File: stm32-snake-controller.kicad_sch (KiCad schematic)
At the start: 46 parts, among them J101 Tag Connector, J102 USB_B_Micro, J103 JST 2.54 Header, J107 Conn_01x02, Q101 AO3501A, SW106 SW_Push, U101 STM32F401RCTx, U102 USBLC6-2SC6, U104 M24C64-RMN, Y101 16MHz, Y103 32.768kHz

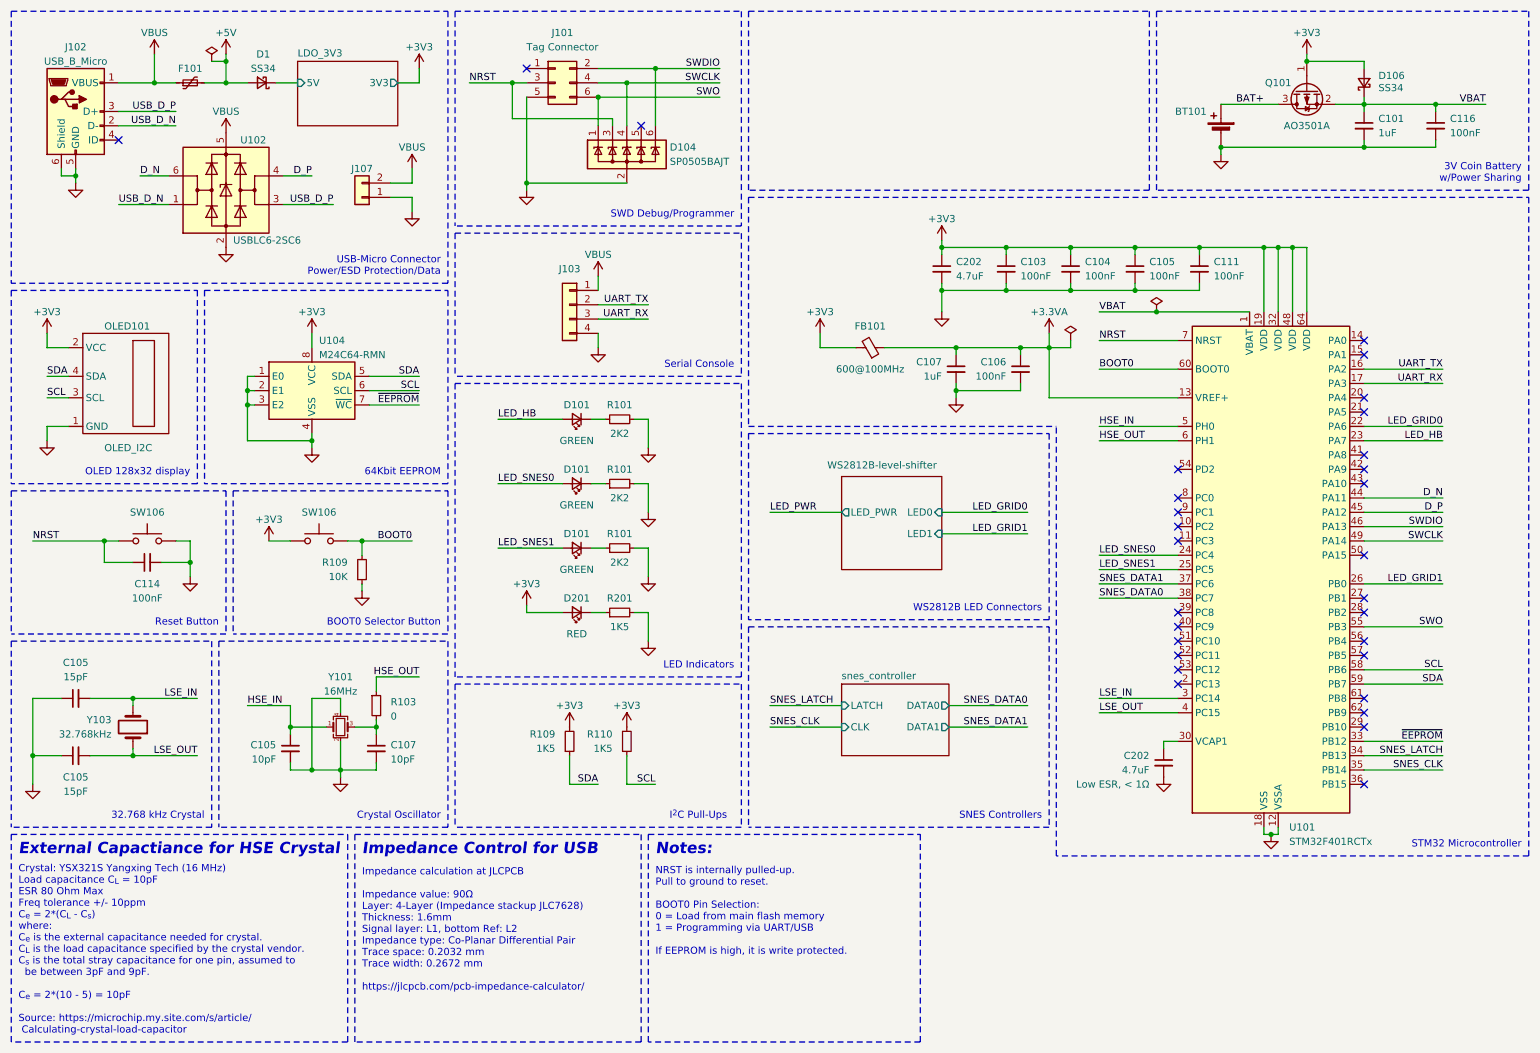
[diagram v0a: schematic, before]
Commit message: update schematic
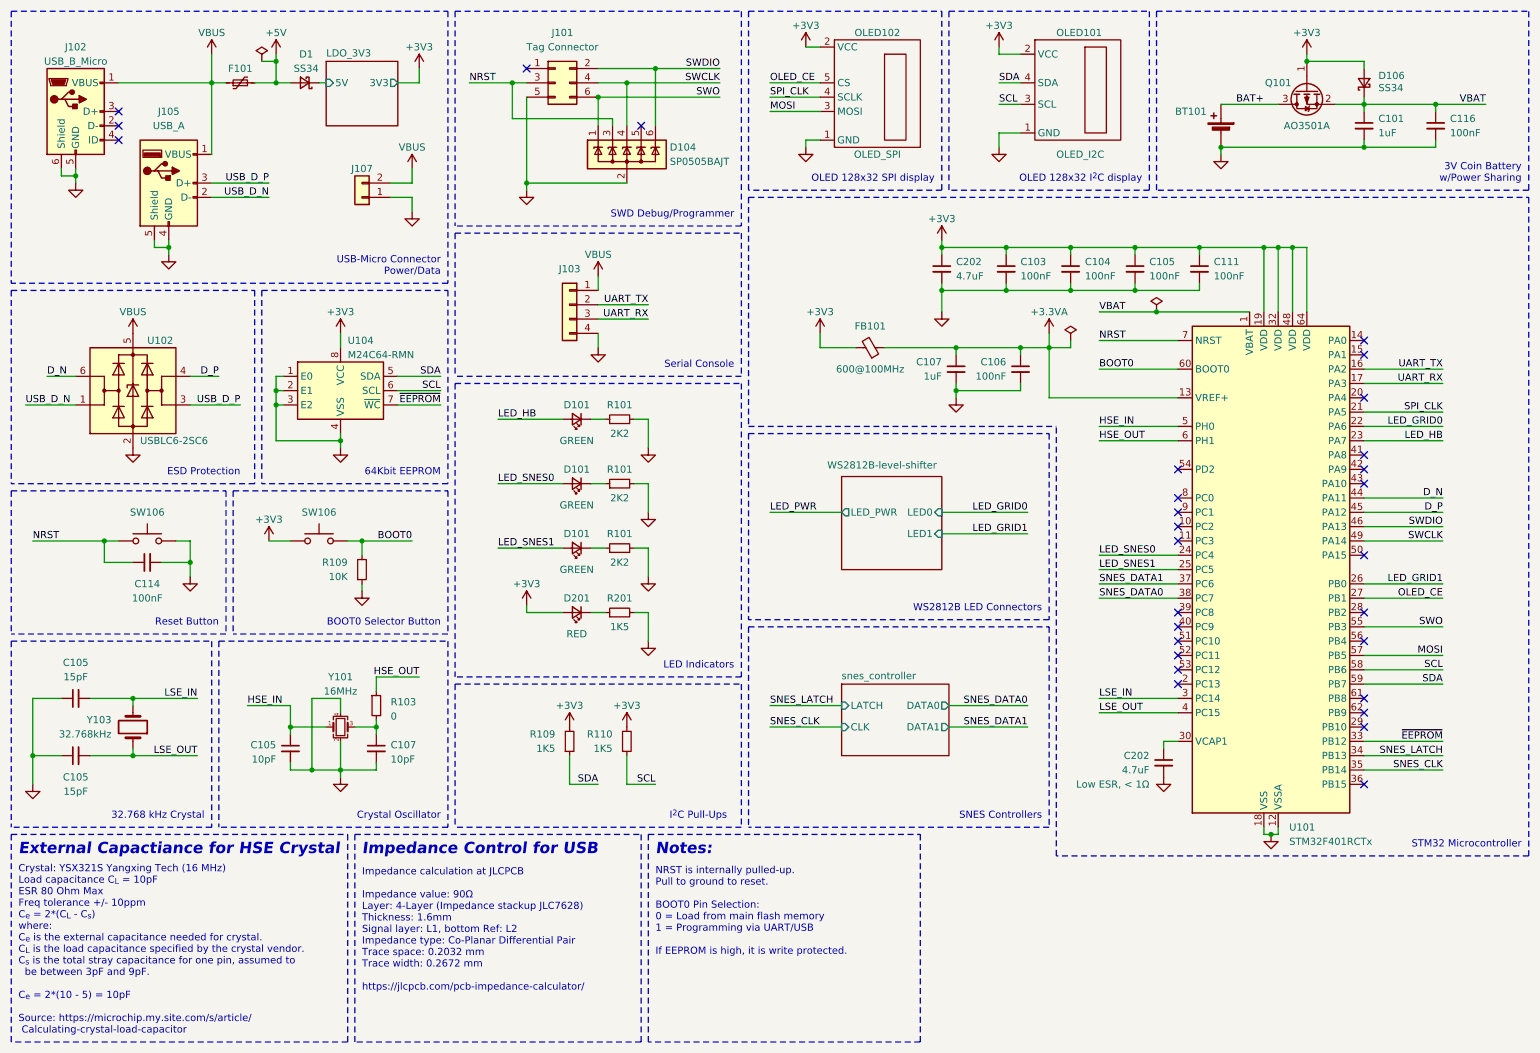
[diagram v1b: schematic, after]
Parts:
- added J105: USB_A, Connector_USB:USB_A_CONNFLY_DS1095-WNR0, symbol Connector:USB_A
- added OLED102: OLED_SPI, Connector_JST:JST_XH_B5B-XH-A_1x05_P2.50mm_Vertical, symbol User Symbols:OLED_SPI
- OLED101: footprint User_Footprint:OLED_128x32_I2C_4pins -> Connector_JST:JST_XH_B4B-XH-A_1x04_P2.50mm_Vertical
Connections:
- net +3V3: now also OLED102.2 (VCC)
- net GND: now also J105.4 (GND), J105.5 (Shield), OLED102.1 (GND)
- net USB_D_N: now also J105.2 (D-); no longer J102.2 (D-)
- net USB_D_P: now also J105.3 (D+); no longer J102.3 (D+)
- net VBUS: now also J105.1 (VBUS)
- net SPI_CLK: now reaches U101.21 (PA5)
- net SPI_CLK: now also OLED102.4 (SCLK)
- net OLED_CE: now reaches U101.27 (PB1)
- net OLED_CE: now also OLED102.5 (CS)
- net MOSI: now reaches U101.57 (PB5)
- net MOSI: now also OLED102.3 (MOSI)
- no-connect marks 30 -> 29
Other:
- note added: "ESD Protection"
- note added: "OLED 128x32 I^{2}C display"
- note added: "OLED 128x32 SPI display"
- note added: "USB-Micro Connector Power/Data"
- note removed: "OLED 128x32 display"
- note removed: "USB-Micro Connector Power/ESD Protection/Data"
- moved on the sheet: D1, F101, OLED101, U102, U104

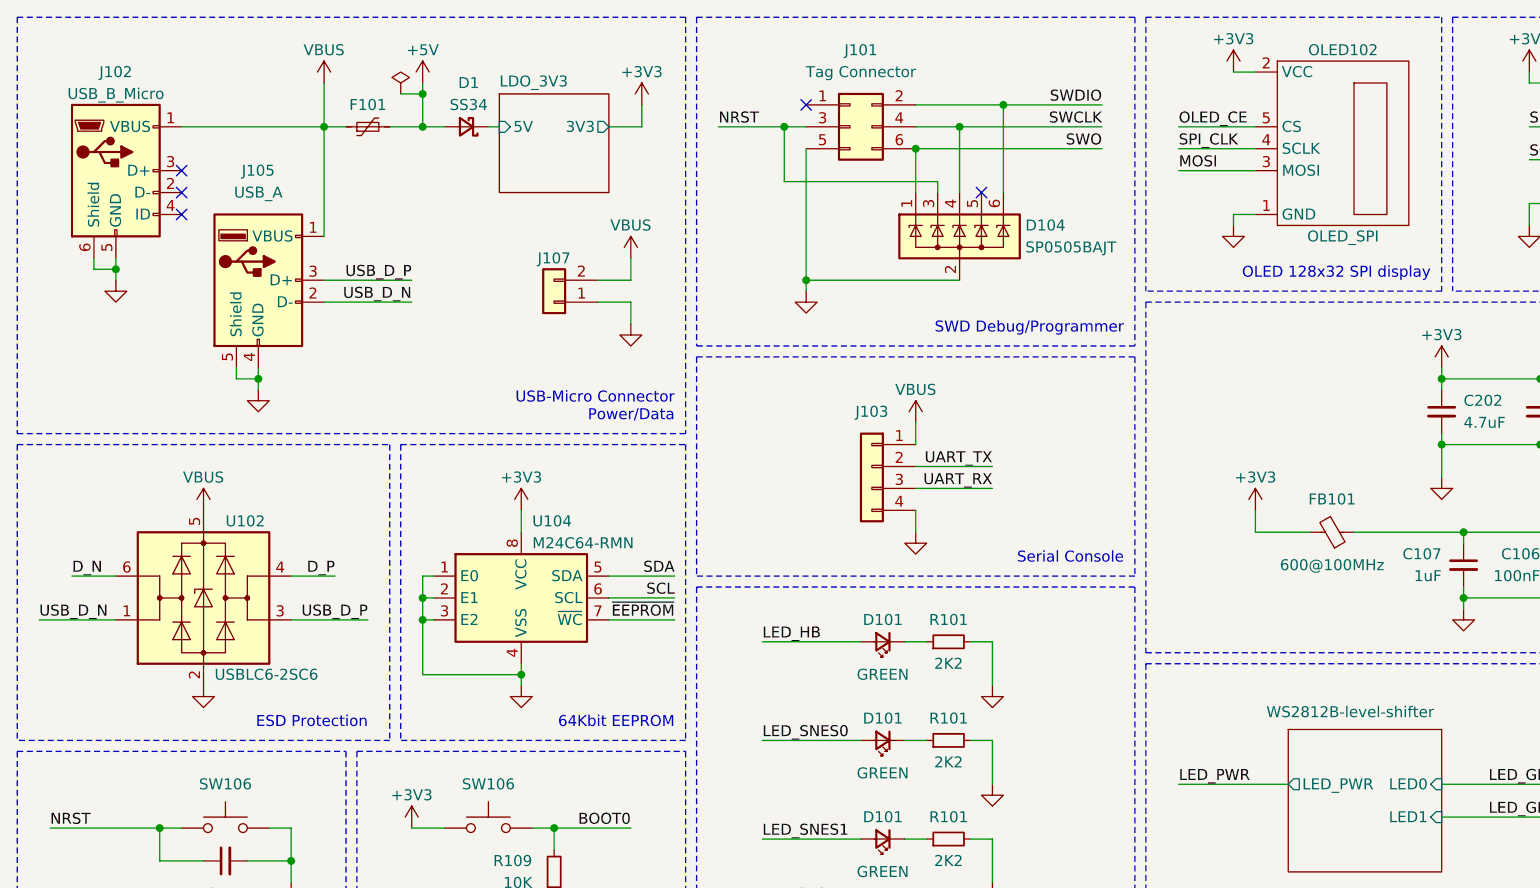
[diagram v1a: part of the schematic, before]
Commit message: replace micro usb to barrel jack
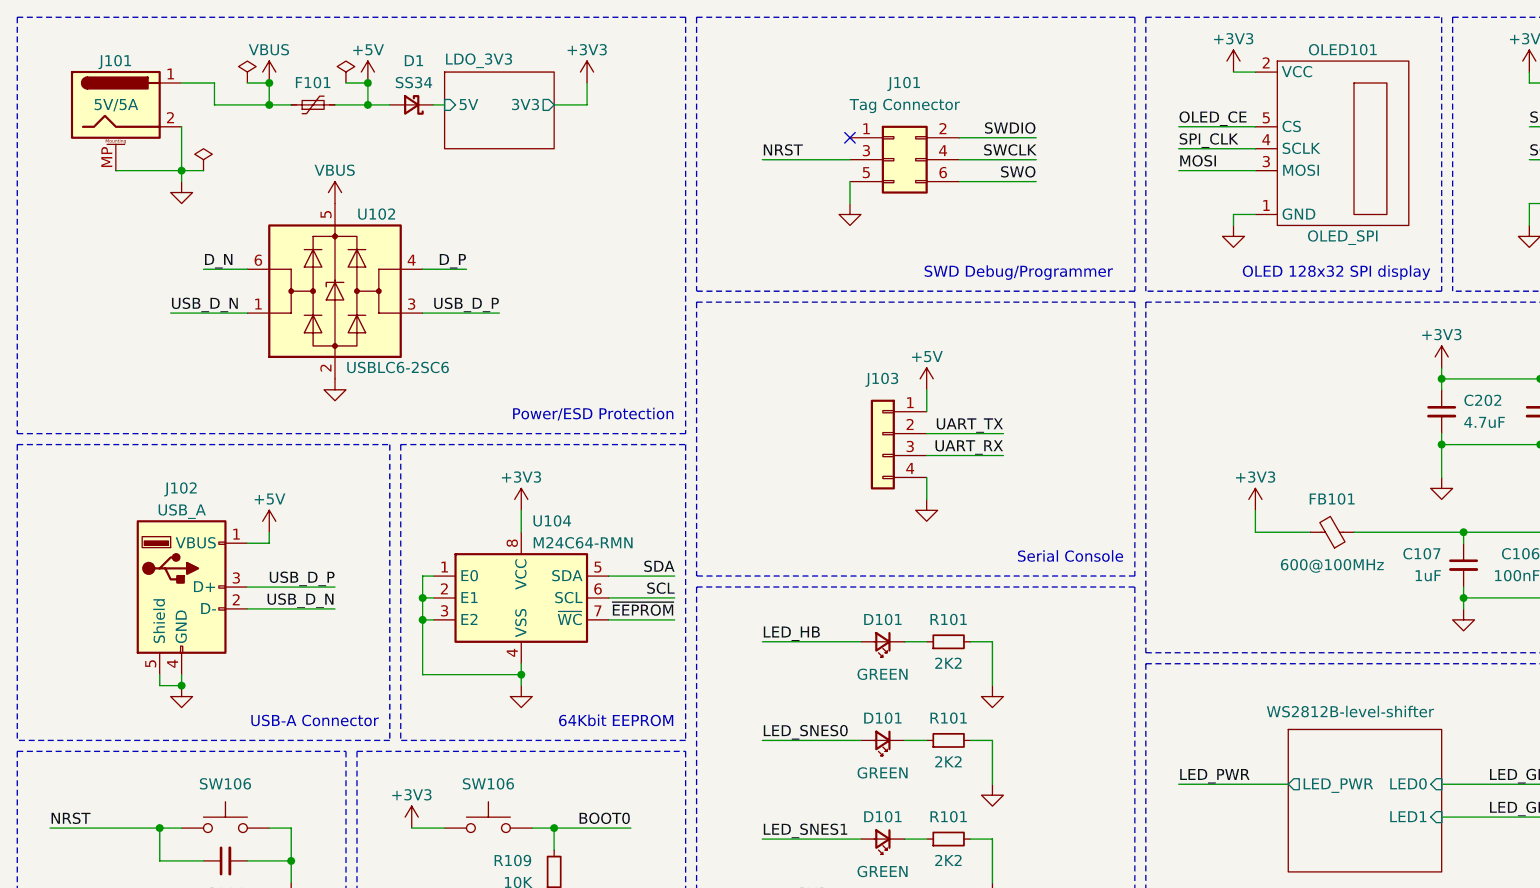
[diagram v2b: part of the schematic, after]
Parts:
- removed D104: SP0505BAJT, Package_TO_SOT_SMD:SOT-363_SC-70-6, symbol Power_Protection:SP0505BAJT
- removed J102: USB_B_Micro, Connector_USB:USB_Micro-B_Molex-105017-0001, symbol Connector:USB_B_Micro
- removed J107: Conn_01x02, Connector_JST:JST_PH_B2B-PH-K_1x02_P2.00mm_Vertical, symbol Connector_Generic:Conn_01x02
- added J101: Barrel_Jack_MountingPin, User_Footprint:DC_Power_Jack_PJ-063BH, symbol Connector:Barrel_Jack_MountingPin
- renumbered J105 to J102, OLED102 to OLED101
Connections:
- net +5V: now also J102.1 (VBUS), J103.1 (Pin_1)
- net GND: now also J101.2, J101.MP (MountPin)
- net VBUS: now also J101.1; no longer J102.1 (VBUS), J103.1 (Pin_1)
- no-connect marks 29 -> 25
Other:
- note added: "Power/ESD Protection"
- note added: "USB-A Connector"
- note removed: "ESD Protection"
- note removed: "USB-Micro Connector Power/Data"
- moved on the sheet: D1, F101, J101, J102, J103, U102
